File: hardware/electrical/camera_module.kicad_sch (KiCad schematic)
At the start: 15 parts, among them U1 XC6228D282VR-G, U3 RT9078-28GJ5

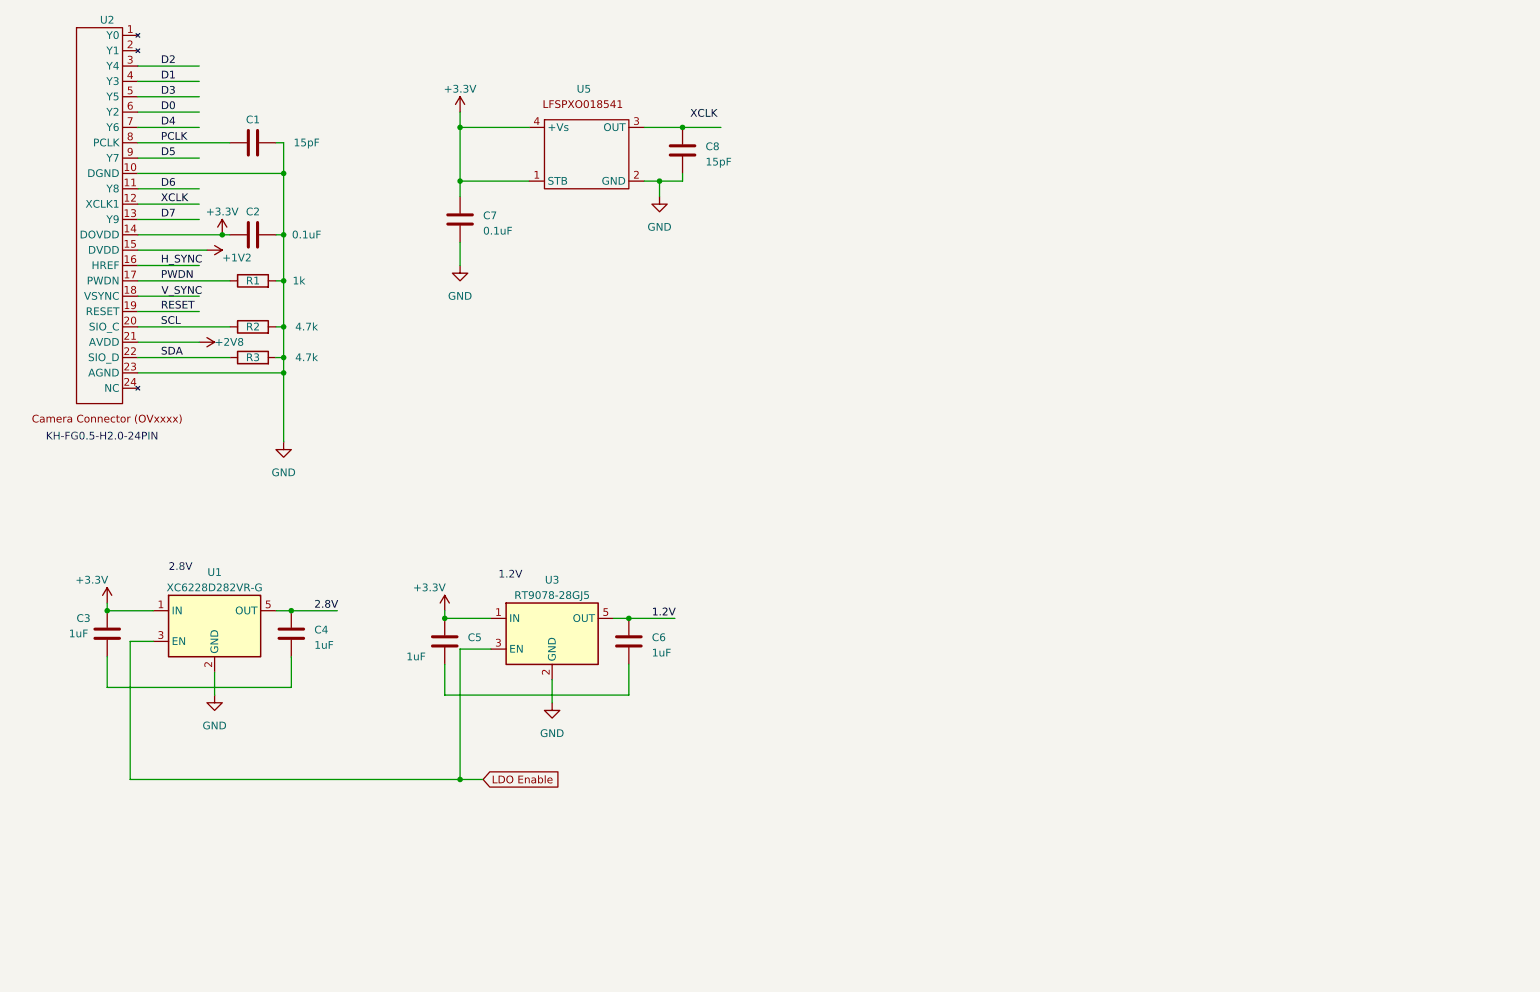
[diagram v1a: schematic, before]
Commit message: Connect camera module to MCU and fix ERC
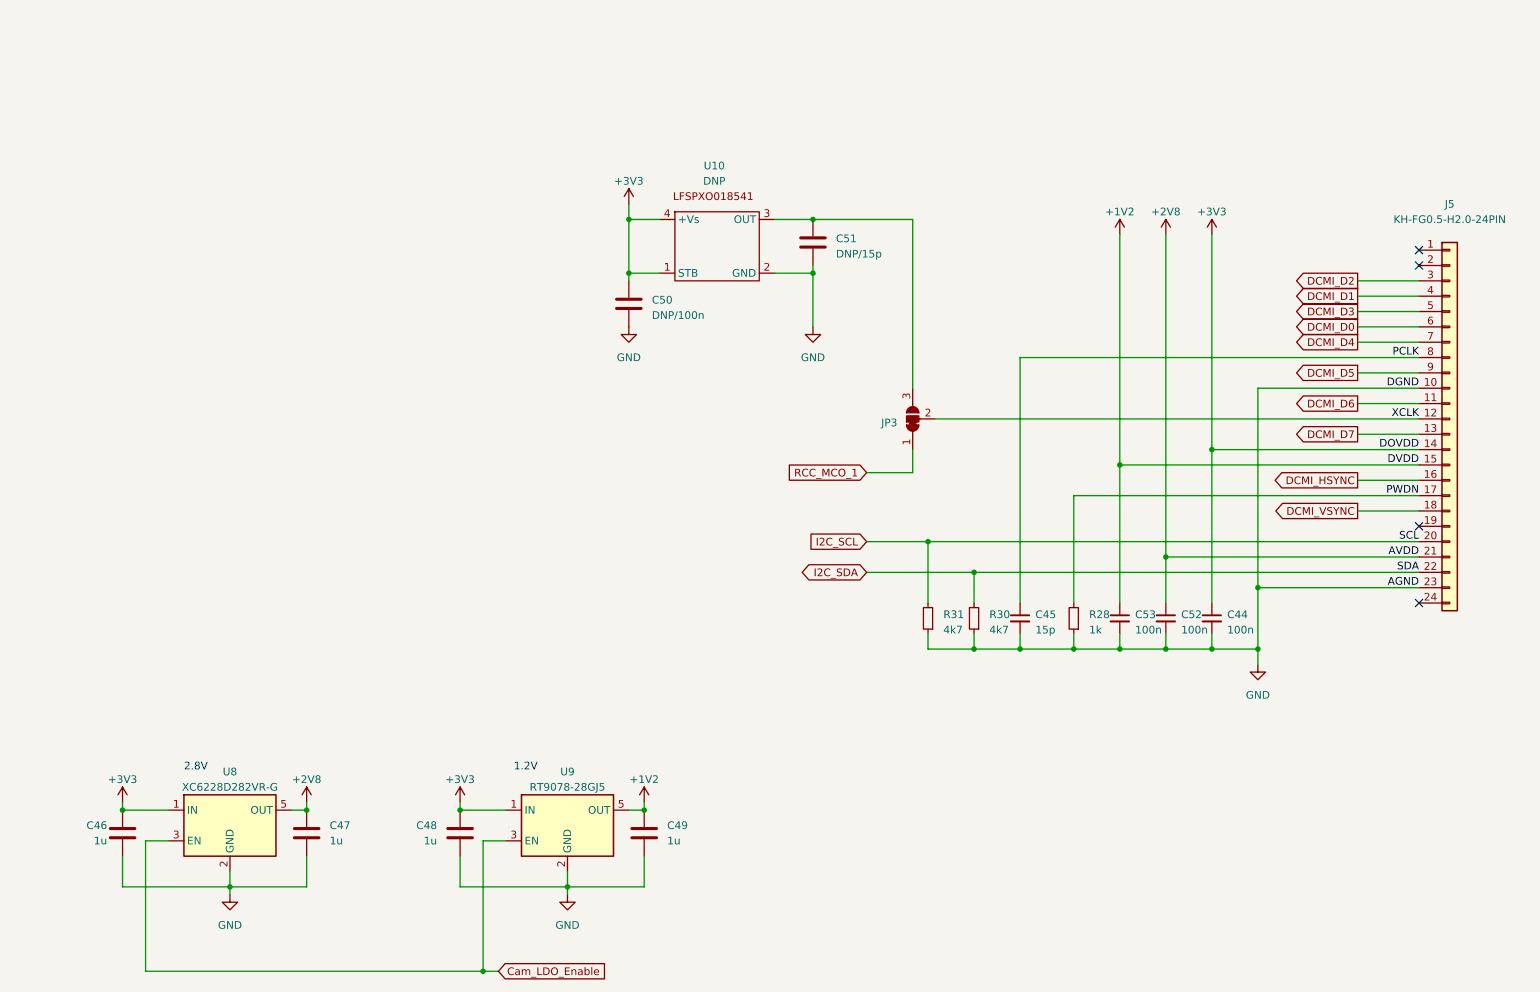
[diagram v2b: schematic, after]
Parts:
- removed C1: 15pF, Capacitor_SMD:C_1206_3216Metric, symbol Device:C
- removed C2: 0.1uF, Capacitor_SMD:C_1206_3216Metric, symbol Device:C
- removed R1: 1k, Resistor_SMD:R_1206_3216Metric, symbol Device:R
- removed R2, R3: 4.7k, Resistor_SMD:R_1206_3216Metric, symbol Device:R
- removed U2: ~, Connector_FFC-FPC:Hirose_FH12-24S-0.5SH_1x24-1MP_P0.50mm_Horizontal, symbol SOL:OV5640
- added C44, C52, C53: 100n, symbol Device:C_Small
- added C45: 15p, symbol Device:C_Small
- added J5: KH-FG0.5-H2.0-24PIN, symbol Connector_Generic:Conn_01x24
- added JP3: SolderJumper_3_Bridged12, symbol Jumper:SolderJumper_3_Bridged12
- added R28: 1k, symbol Device:R_Small
- added R30, R31: 4k7, symbol Device:R_Small
- C46: renamed from C3; value 1uF -> 1u
- C47: renamed from C4; value 1uF -> 1u
- C48: renamed from C5; value 1uF -> 1u
- C49: renamed from C6; value 1uF -> 1u
- C50: renamed from C7; value 0.1uF -> DNP/100n
- C51: renamed from C8; value 15pF -> DNP/15p
- U10: renamed from U5; value ~ -> DNP
- renumbered U1 to U8, U3 to U9
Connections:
- net 2.8V is gone; now on net +2V8: C47.1, U8.5 (OUT)
- net +2V8: now also C52.1, J5.21 (Pin_21)
- net GND: now also C46.2, C47.2, C48.2, C49.2, C44.2, C45.2, C52.2, C53.2, J5.10 (Pin_10), J5.23 (Pin_23), R28.1, R30.1, R31.1
- net PCLK: now also C45.1, J5.8 (Pin_8)
- net PWDN: now also J5.17 (Pin_17), R28.2
- net XCLK: now also J5.12 (Pin_12), JP3.2 (C)
- net at C51.1, U10.3 (OUT): now also JP3.3 (B)
- net +3.3V renamed +3V3
- net +3V3: now also C44.1, J5.14 (Pin_14)
- net 1.2V renamed +1V2
- net +1V2: now also C53.1, J5.15 (Pin_15)
- net LDO Enable renamed Cam_LDO_Enable
- new net DCMI_D0: J5.6 (Pin_6)
- new net DCMI_D1: J5.4 (Pin_4)
- new net DCMI_D2: J5.3 (Pin_3)
- new net DCMI_D3: J5.5 (Pin_5)
- new net DCMI_D4: J5.7 (Pin_7)
- new net DCMI_D5: J5.9 (Pin_9)
- new net DCMI_D6: J5.11 (Pin_11)
- new net DCMI_D7: J5.13 (Pin_13)
- new net DCMI_HSYNC: J5.16 (Pin_16)
- new net DCMI_VSYNC: J5.18 (Pin_18)
- new net I2C_SCL: J5.20 (Pin_20), R31.2
- new net I2C_SDA: J5.22 (Pin_22), R30.2
- new net RCC_MCO_1: JP3.1 (A)
- no-connect marks 0 -> 4
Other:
- note removed: "KH-FG0.5-H2.0-24PIN"
- company: (none) -> Sol Harter
- title: (none) -> Camera Module
- moved on the sheet: C46, C47, C48, C49, C50, C51, U10, U8, U9

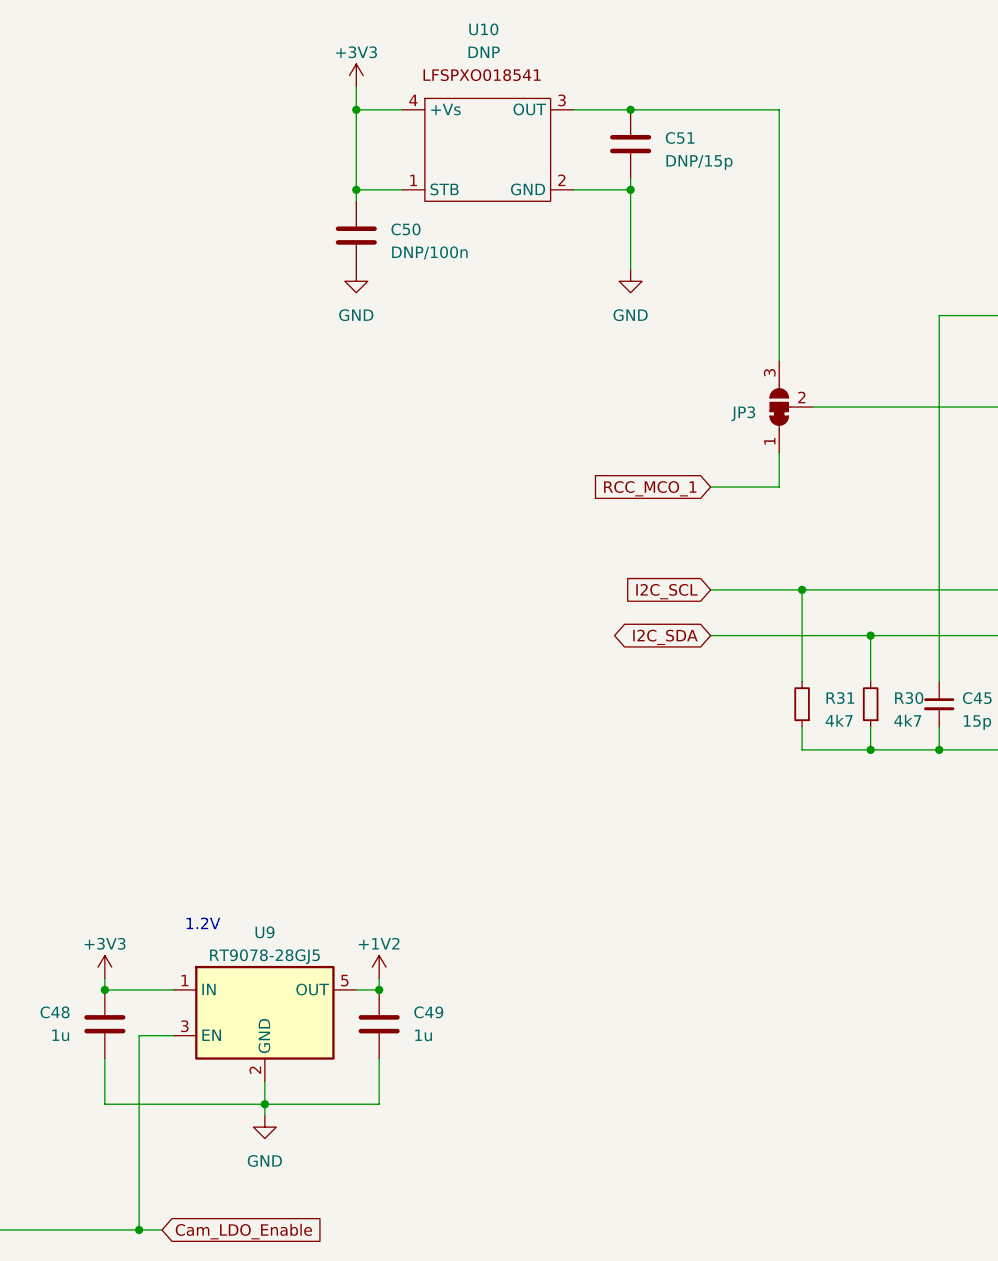
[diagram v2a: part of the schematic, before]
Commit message: Replace LFSPXO018541 with SG-210STF
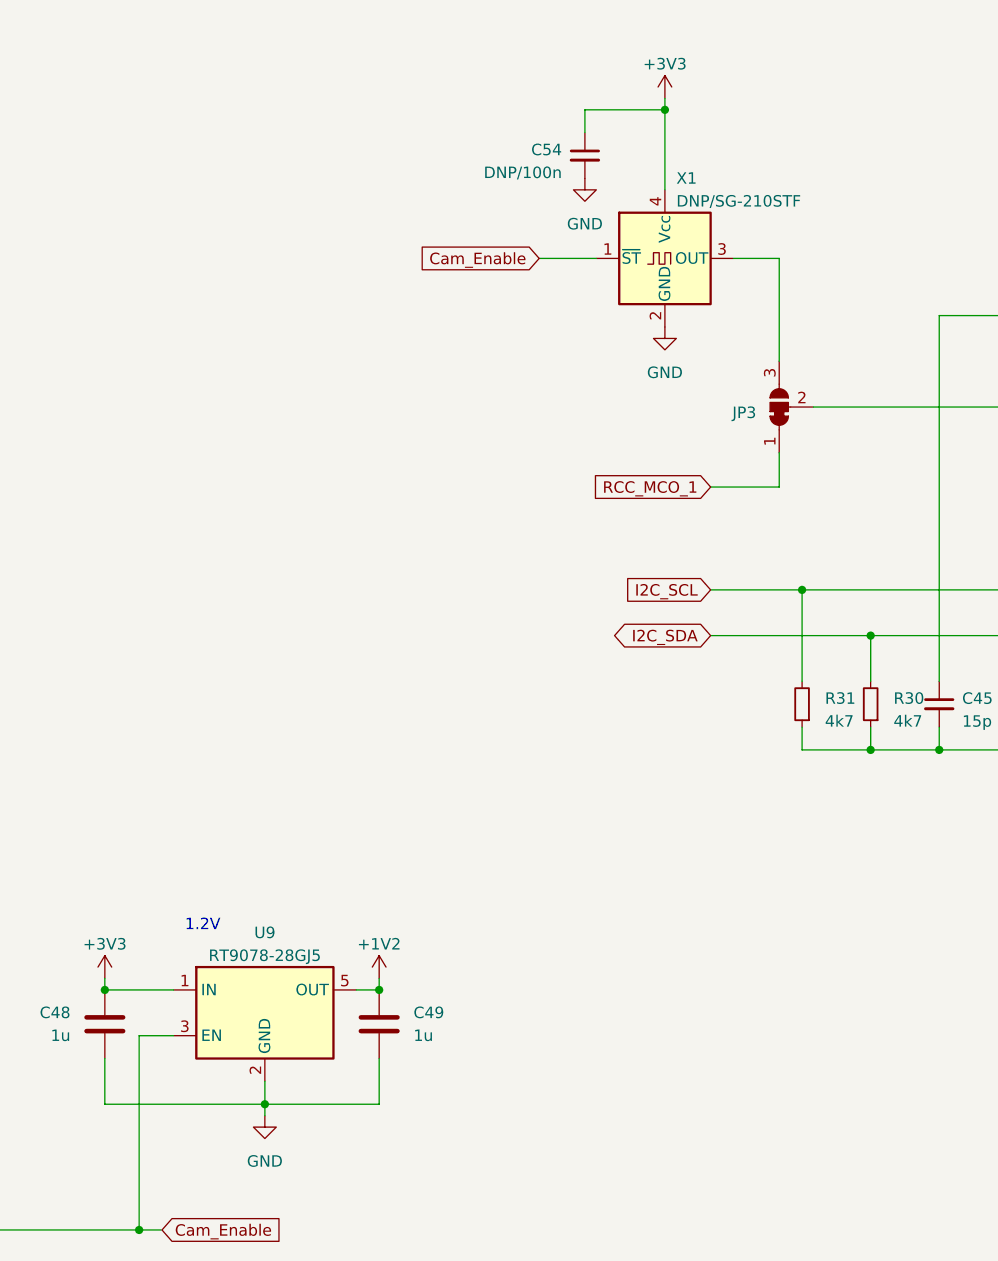
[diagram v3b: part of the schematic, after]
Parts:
- removed C50: DNP/100n, Capacitor_SMD:C_1206_3216Metric, symbol Device:C
- removed C51: DNP/15p, Capacitor_SMD:C_1206_3216Metric, symbol Device:C
- removed U10: DNP, Oscillator:Oscillator_SMD_SeikoEpson_SG8002CA-4Pin_7.0x5.0mm, symbol SOL:LFSPXO018541
- added C54: DNP/100n, symbol Device:C_Small
- added X1: DNP/SG-210STF, Oscillator:Oscillator_SMD_SeikoEpson_SG210-4Pin_2.5x2.0mm, symbol Oscillator:SG-210STF
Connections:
- net +3V3: now also C54.1, X1.4 (Vcc)
- net GND: now also C54.2, X1.2 (GND)
- net at JP3.3 (B): now also X1.3 (OUT)
- net Cam_LDO_Enable renamed Cam_Enable
- net Cam_Enable: now also X1.1 (~{ST})
